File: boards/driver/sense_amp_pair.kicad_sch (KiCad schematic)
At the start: 18 parts, among them T15 1:1, T16 1:1, U9 SN7524

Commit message: Driver: Added a 5V->3.3V LDO to replace the reversed cmod header, added jumpers for the 200R parallel returns, and renamed subcircuit ports to avoid unexpected ground connections.
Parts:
- renumbered C32 to C41, C33 to C42, C34 to C43, C35 to C44, R59 to R241, R60 to R242, R61 to R243, R62 to R244, R63 to R245, R64 to R246, R65 to R247, R66 to R248, U9 to U8
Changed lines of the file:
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@@
   (symbol (lib_id "Device:R_US") (at 73.66 46.99 0)
     (in_bom yes) (on_board yes)
-    (property "Reference" "R59" (id 0) (at 75.3872 45.8216 0)
+    (property "Reference" "R241" (id 0) (at 75.3872 45.8216 0)
       (effects (font (size 1.27 1.27)) (justify left))
     )
@@
   (symbol (lib_id "Device:R_US") (at 73.66 57.15 0)
     (in_bom yes) (on_board yes)
-    (property "Reference" "R60" (id 0) (at 75.3872 55.9816 0)
+    (property "Reference" "R242" (id 0) (at 75.3872 55.9816 0)
       (effects (font (size 1.27 1.27)) (justify left))
     )
@@
   (symbol (lib_id "Device:R_US") (at 111.76 46.99 0) (mirror y)
     (in_bom yes) (on_board yes)
-    (property "Reference" "R63" (id 0) (at 106.68 45.72 0)
+    (property "Reference" "R245" (id 0) (at 106.68 45.72 0)
       (effects (font (size 1.27 1.27)) (justify right))
     )
@@
   (symbol (lib_id "Device:R_US") (at 111.76 57.15 0) (mirror y)
     (in_bom yes) (on_board yes)
-    (property "Reference" "R64" (id 0) (at 106.68 55.88 0)
+    (property "Reference" "R246" (id 0) (at 106.68 55.88 0)
       (effects (font (size 1.27 1.27)) (justify right))
     )
@@
   (symbol (lib_id "power:GND") (at 116.84 54.61 0)
     (in_bom yes) (on_board yes)
-    (property "Reference" "#PWR049" (id 0) (at 116.84 60.96 0)
+    (property "Reference" "#PWR0115" (id 0) (at 116.84 60.96 0)
       (effects (font (size 1.27 1.27)) hide)
     )
@@
   (symbol (lib_id "lachesis:SN7524") (at 142.24 52.07 0)
     (in_bom yes) (on_board yes)
-    (property "Reference" "U9" (id 0) (at 142.24 42.7482 0))
+    (property "Reference" "U8" (id 0) (at 142.24 42.7482 0))
     (property "Value" "SN7524" (id 1) (at 142.24 45.0596 0))
     (property "Footprint" "Package_DIP:DIP-16_W7.62mm_Socket" (id 2) (at 142.24 52.07 0)
@@
   (symbol (lib_id "Device:R_US") (at 73.66 72.39 0)
     (in_bom yes) (on_board yes)
-    (property "Reference" "R61" (id 0) (at 75.3872 71.2216 0)
+    (property "Reference" "R243" (id 0) (at 75.3872 71.2216 0)
       (effects (font (size 1.27 1.27)) (justify left))
     )
@@
   (symbol (lib_id "Device:R_US") (at 73.66 82.55 0)
     (in_bom yes) (on_board yes)
-    (property "Reference" "R62" (id 0) (at 75.3872 81.3816 0)
+    (property "Reference" "R244" (id 0) (at 75.3872 81.3816 0)
       (effects (font (size 1.27 1.27)) (justify left))
     )
@@
   (symbol (lib_id "Device:R_US") (at 111.76 72.39 0) (mirror y)
     (in_bom yes) (on_board yes)
-    (property "Reference" "R65" (id 0) (at 106.68 71.12 0)
+    (property "Reference" "R247" (id 0) (at 106.68 71.12 0)
       (effects (font (size 1.27 1.27)) (justify right))
     )
@@
   (symbol (lib_id "Device:R_US") (at 111.76 82.55 0) (mirror y)
     (in_bom yes) (on_board yes)
-    (property "Reference" "R66" (id 0) (at 106.68 81.28 0)
+    (property "Reference" "R248" (id 0) (at 106.68 81.28 0)
       (effects (font (size 1.27 1.27)) (justify right))
     )
@@
   (symbol (lib_id "power:GND") (at 116.84 80.01 0)
     (in_bom yes) (on_board yes)
-    (property "Reference" "#PWR050" (id 0) (at 116.84 86.36 0)
+    (property "Reference" "#PWR0116" (id 0) (at 116.84 86.36 0)
       (effects (font (size 1.27 1.27)) hide)
     )
@@
   (symbol (lib_id "lachesis:SN7524") (at 142.24 77.47 0)
     (in_bom yes) (on_board yes)
-    (property "Reference" "U9" (id 0) (at 142.24 68.1482 0))
+    (property "Reference" "U8" (id 0) (at 142.24 68.1482 0))
     (property "Value" "SN7524" (id 1) (at 142.24 70.4596 0))
     (property "Footprint" "Package_DIP:DIP-16_W7.62mm_Socket" (id 2) (at 142.24 77.47 0)
@@
       (effects (font (size 1.27 1.27)) hide)
     )
-    (pin "14")
-    (pin "15")
-    (pin "2")
-    (pin "3")
+    (pin "11")
+    (pin "12")
+    (pin "6")
+    (pin "7")
   )
   (symbol (lib_id "lachesis:Transformer_SP_SS") (at 92.71 77.47 0) (mirror x)
@@
   (symbol (lib_id "lachesis:SN7524") (at 205.74 85.09 0)
     (in_bom yes) (on_board yes)
-    (property "Reference" "U9" (id 0) (at 204.47 92.71 0)
+    (property "Reference" "U8" (id 0) (at 204.47 92.71 0)
       (effects (font (size 1.27 1.27)) (justify left))
     )
@@
       (effects (font (size 1.27 1.27)) hide)
     )
-    (pin "14")
-    (pin "15")
-    (pin "2")
-    (pin "3")
+    (pin "1")
+    (pin "10")
+    (pin "13")
+    (pin "16")
+    (pin "8")
+    (pin "9")
   )
   (symbol (lib_id "power:GND") (at 217.17 90.17 0)
     (in_bom yes) (on_board yes)
-    (property "Reference" "#PWR054" (id 0) (at 217.17 96.52 0)
+    (property "Reference" "#PWR0120" (id 0) (at 217.17 96.52 0)
       (effects (font (size 1.27 1.27)) hide)
     )
@@
   (symbol (lib_id "Device:C_Small") (at 217.17 85.09 180)
     (in_bom yes) (on_board yes)
-    (property "Reference" "C33" (id 0) (at 219.4814 83.9216 0)
+    (property "Reference" "C42" (id 0) (at 219.4814 83.9216 0)
       (effects (font (size 1.27 1.27)) (justify right))
     )
@@
   (symbol (lib_id "Device:C_Small") (at 226.06 81.28 0) (mirror y)
     (in_bom yes) (on_board yes)
-    (property "Reference" "C34" (id 0) (at 228.3968 82.4484 0)
+    (property "Reference" "C43" (id 0) (at 228.3968 82.4484 0)
       (effects (font (size 1.27 1.27)) (justify right))
     )
@@
   (symbol (lib_id "Device:C_Small") (at 226.06 93.98 0) (mirror y)
     (in_bom yes) (on_board yes)
-    (property "Reference" "C35" (id 0) (at 228.3968 95.1484 0)
+    (property "Reference" "C44" (id 0) (at 228.3968 95.1484 0)
       (effects (font (size 1.27 1.27)) (justify right))
     )
@@
   (symbol (lib_id "lachesis:SN7524") (at 140.97 113.03 0)
     (in_bom yes) (on_board yes)
-    (property "Reference" "U9" (id 0) (at 146.05 115.57 0))
+    (property "Reference" "U8" (id 0) (at 146.05 115.57 0))
     (property "Value" "SN7524" (id 1) (at 144.78 118.11 0))
     (property "Footprint" "Package_DIP:DIP-16_W7.62mm_Socket" (id 2) (at 140.97 113.03 0)
@@
       (effects (font (size 1.27 1.27)) hide)
     )
-    (pin "14")
-    (pin "15")
-    (pin "2")
-    (pin "3")
+    (pin "4")
+    (pin "5")
   )
   (symbol (lib_id "Device:C_Small") (at 129.54 113.03 0) (mirror x)
     (in_bom yes) (on_board yes)
-    (property "Reference" "C32" (id 0) (at 127.2286 111.8616 0)
+    (property "Reference" "C41" (id 0) (at 127.2286 111.8616 0)
       (effects (font (size 1.27 1.27)) (justify right))
     )
@@
   (symbol (lib_id "power:GND") (at 120.65 118.11 0)
     (in_bom yes) (on_board yes)
-    (property "Reference" "#PWR051" (id 0) (at 120.65 124.46 0)
+    (property "Reference" "#PWR0117" (id 0) (at 120.65 124.46 0)
       (effects (font (size 1.27 1.27)) hide)
     )
@@
   (symbol (lib_id "power:+5V") (at 203.2 72.39 0)
     (in_bom yes) (on_board yes)
-    (property "Reference" "#PWR052" (id 0) (at 203.2 76.2 0)
+    (property "Reference" "#PWR0118" (id 0) (at 203.2 76.2 0)
       (effects (font (size 1.27 1.27)) hide)
     )
@@
   (symbol (lib_id "power:-5V") (at 203.2 100.33 180)
     (in_bom yes) (on_board yes)
-    (property "Reference" "#PWR053" (id 0) (at 203.2 102.87 0)
-      (effects (font (size 1.27 1.27)) hide)
-    )
+    (property "Reference" "#PWR0119" (id 0) (at 203.2 102.87 0)
+      (effects (font (size 1.27 1.27)) hide)
+    )

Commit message: Driver: incorporated most changes from the test board, and began layout
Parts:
- C13: renamed from C41; value 10nF -> 0.01uF
- C15: renamed from C43; value 0.1uF -> 0.01uF
- C16: renamed from C44; value 0.1uF -> 0.01uF
- R189: renamed from R245; value 470 -> 100
- R190: renamed from R246; value 470 -> 100
- R191: renamed from R247; value 470 -> 100
- R192: renamed from R248; value 470 -> 100
- renumbered C42 to C14, R241 to R185, R242 to R186, R243 to R187, R244 to R188, T15 to T1, T16 to T2, U8 to U1
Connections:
- net +5V: now also U1.16 (VCC+)
- net -5V: now also U1.8 (VCC-)
- net GND: now also U1.13 (GND), U1.4 (-), U1.9 (GND); no longer U1.3
- net SAY: now also U1.12; no longer U1.14
- net SBF: now also U1.11; no longer U1.15
- net VREF: now also U1.5 (+); no longer U1.2
- net at R191.1, T2.4 (S2): now also U1.6; no longer U1.2
- net at R192.2, T2.6 (S1): now also U1.7; no longer U1.3
- net at C14.2: now also U1.1 (CEXT)

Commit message: Driver: laid out most of the subcircuits
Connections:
- net GARX: now also R187.1, T2.3 (P2); no longer R185.1, T1.3 (P2)
- net GARY: now also R185.1, T1.3 (P2); no longer R187.1, T2.3 (P2)
- net GBRX: now also R188.2, T2.1 (P1); no longer R186.2, T1.1 (P1)
- net GBRY: now also R186.2, T1.1 (P1); no longer R188.2, T2.1 (P1)
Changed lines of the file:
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@@
     (effects (font (size 1.27 1.27)) (justify right))
   )
-  (hierarchical_label "GARY" (shape input) (at 67.31 67.31 180)
+  (hierarchical_label "GARY" (shape input) (at 66.04 41.91 180)
     (effects (font (size 1.27 1.27)) (justify right))
   )
-  (hierarchical_label "GARX" (shape input) (at 66.04 41.91 180)
+  (hierarchical_label "GARX" (shape input) (at 67.31 67.31 180)
     (effects (font (size 1.27 1.27)) (justify right))
   )
-  (hierarchical_label "GBRX" (shape input) (at 67.31 62.23 180)
+  (hierarchical_label "GBRX" (shape input) (at 68.58 87.63 180)
     (effects (font (size 1.27 1.27)) (justify right))
   )
-  (hierarchical_label "GBRY" (shape input) (at 68.58 87.63 180)
+  (hierarchical_label "GBRY" (shape input) (at 67.31 62.23 180)
     (effects (font (size 1.27 1.27)) (justify right))
   )

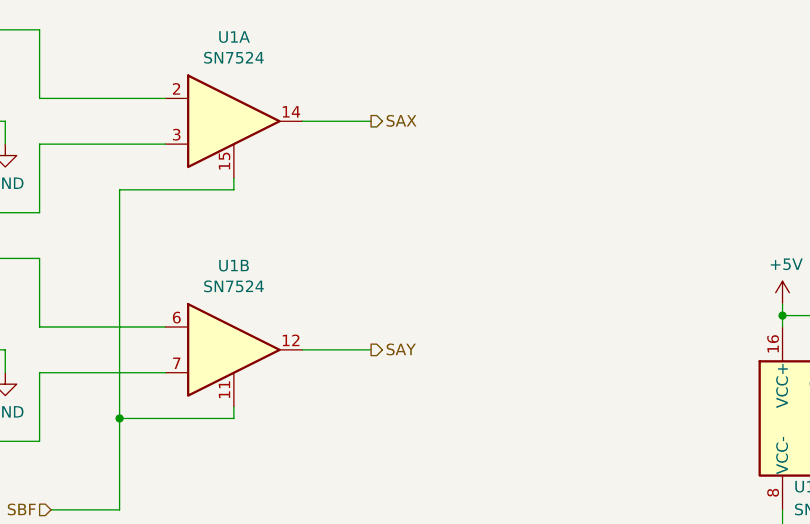
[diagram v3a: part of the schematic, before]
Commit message: Driver: almost totally rearranged 3.3V logic section. The ratsnest is now significantly detangled, and the FPGA routing is almost done. 89 nets left.
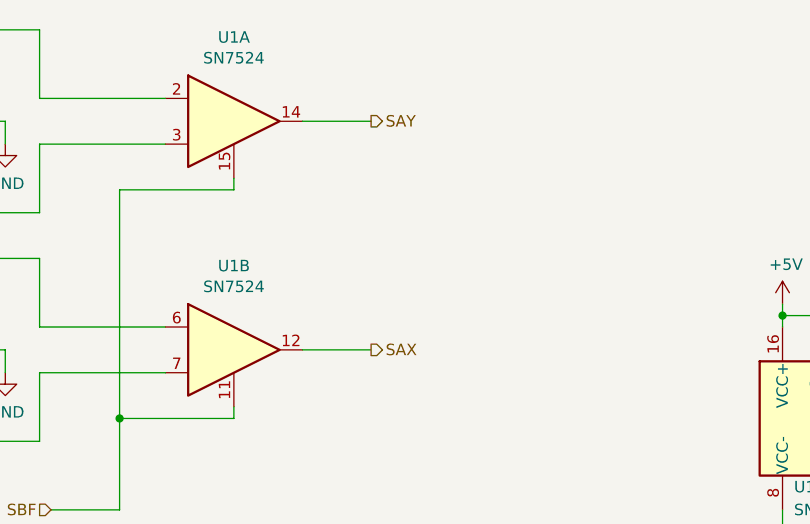
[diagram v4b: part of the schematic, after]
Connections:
- net SAX: now also U1.12; no longer U1.14
- net SAY: now also U1.14; no longer U1.12
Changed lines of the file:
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@@
     (effects (font (size 1.27 1.27)) (justify right))
   )
-  (hierarchical_label "SAY" (shape output) (at 157.48 77.47 0)
+  (hierarchical_label "SAY" (shape output) (at 157.48 52.07 0)
     (effects (font (size 1.27 1.27)) (justify left))
   )
-  (hierarchical_label "SAX" (shape output) (at 157.48 52.07 0)
+  (hierarchical_label "SAX" (shape output) (at 157.48 77.47 0)
     (effects (font (size 1.27 1.27)) (justify left))
   )

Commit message: Driver: minor schematic cleanup and populated all of the BOM except for resistors
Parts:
- C13: MPN (none) -> CL10B103KC8NNNC; Manufacturer (none) -> Samsung Electro-Mechanics; Package (none) -> 0603
- C14: MPN (none) -> CL10B101KB8NFNC; Manufacturer (none) -> Samsung Electro-Mechanics; Package (none) -> 0603
- C15, C16: MPN (none) -> CL10B103KC8NNNC; Manufacturer (none) -> Samsung Electro-Mechanics; Package (none) -> 0603; Rating (none) -> 100V; Tolerance (none) -> 10%
- T1, T2: MPN (none) -> 78615/1JC; Manufacturer (none) -> Murata Power Solutions, Inc; Package (none) -> 6 PIN SM
- U1: MPN (none) -> 110-93-316-41-001000; Manufacturer (none) -> Mill-Max Manufacturing Corp; Package (none) -> 16-DIP
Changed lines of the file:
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@@
+      (effects (font (size 1.27 1.27)) hide)
+    )
+    (property "MPN" "110-93-316-41-001000" (id 4) (at 142.24 52.07 0)
+      (effects (font (size 1.27 1.27)) hide)
+    )
+    (property "Description" "CONN IC DIP SOCKET 16POS GOLD" (id 5) (at 142.24 52.07 0)
+      (effects (font (size 1.27 1.27)) hide)
+    )
+    (property "Manufacturer" "Mill-Max Manufacturing Corp" (id 6) (at 142.24 52.07 0)
+      (effects (font (size 1.27 1.27)) hide)
+    )
+    (property "Package" "16-DIP" (id 7) (at 142.24 52.07 0)
       (effects (font (size 1.27 1.27)) hide)
     )
@@
       (effects (font (size 1.27 1.27)) hide)
     )
+    (property "MPN" "78615/1JC" (id 6) (at 92.71 52.07 0)
+      (effects (font (size 1.27 1.27)) hide)
+    )
+    (property "Manufacturer" "Murata Power Solutions, Inc" (id 7) (at 92.71 52.07 0)
+      (effects (font (size 1.27 1.27)) hide)
+    )
+    (property "Description" "PULSE XFMR 1CT:1CT 1.7MH" (id 8) (at 92.71 52.07 0)
+      (effects (font (size 1.27 1.27)) hide)
+    )
+    (property "Package" "6 PIN SM" (id 9) (at 92.71 52.07 0)
+      (effects (font (size 1.27 1.27)) hide)
+    )
     (pin "1")
     (pin "2")
@@
     )
     (property "Datasheet" "" (id 3) (at 142.24 77.47 0)
+      (effects (font (size 1.27 1.27)) hide)
+    )
+    (property "MPN" "110-93-316-41-001000" (id 4) (at 142.24 77.47 0)
+      (effects (font (size 1.27 1.27)) hide)
+    )
+    (property "Description" "CONN IC DIP SOCKET 16POS GOLD" (id 5) (at 142.24 77.47 0)
+      (effects (font (size 1.27 1.27)) hide)
+    )
+    (property "Manufacturer" "Mill-Max Manufacturing Corp" (id 6) (at 142.24 77.47 0)
+      (effects (font (size 1.27 1.27)) hide)
+    )
+    (property "Package" "16-DIP" (id 7) (at 142.24 77.47 0)
       (effects (font (size 1.27 1.27)) hide)
     )
@@
       (effects (font (size 1.27 1.27)) hide)
     )
+    (property "MPN" "78615/1JC" (id 6) (at 92.71 77.47 0)
+      (effects (font (size 1.27 1.27)) hide)
+    )
+    (property "Manufacturer" "Murata Power Solutions, Inc" (id 7) (at 92.71 77.47 0)
+      (effects (font (size 1.27 1.27)) hide)
+    )
+    (property "Description" "PULSE XFMR 1CT:1CT 1.7MH" (id 8) (at 92.71 77.47 0)
+      (effects (font (size 1.27 1.27)) hide)
+    )
+    (property "Package" "6 PIN SM" (id 9) (at 92.71 77.47 0)
+      (effects (font (size 1.27 1.27)) hide)
+    )
     (pin "1")
     (pin "2")
@@
     )
     (property "Datasheet" "" (id 3) (at 205.74 85.09 0)
+      (effects (font (size 1.27 1.27)) hide)
+    )
+    (property "MPN" "110-93-316-41-001000" (id 4) (at 205.74 85.09 0)
+      (effects (font (size 1.27 1.27)) hide)
+    )
+    (property "Description" "CONN IC DIP SOCKET 16POS GOLD" (id 5) (at 205.74 85.09 0)
+      (effects (font (size 1.27 1.27)) hide)
+    )
+    (property "Manufacturer" "Mill-Max Manufacturing Corp" (id 6) (at 205.74 85.09 0)
+      (effects (font (size 1.27 1.27)) hide)
+    )
+    (property "Package" "16-DIP" (id 7) (at 205.74 85.09 0)
       (effects (font (size 1.27 1.27)) hide)
     )
@@
       (effects (font (size 1.27 1.27)) hide)
     )
+    (property "Description" "CAP CER 100PF 50V X7R 0603" (id 8) (at 217.17 85.09 0)
+      (effects (font (size 1.27 1.27)) hide)
+    )
+    (property "MPN" "CL10B101KB8NFNC" (id 9) (at 217.17 85.09 0)
+      (effects (font (size 1.27 1.27)) hide)
+    )
+    (property "Manufacturer" "Samsung Electro-Mechanics" (id 10) (at 217.17 85.09 0)
+      (effects (font (size 1.27 1.27)) hide)
+    )
+    (property "Package" "0603" (id 11) (at 217.17 85.09 0)
+      (effects (font (size 1.27 1.27)) hide)
+    )
     (pin "1")
     (pin "2")
@@
       (effects (font (size 1.27 1.27)) hide)
     )
+    (property "Rating" "100V" (id 4) (at 226.06 81.28 0)
+      (effects (font (size 1.27 1.27)) hide)
+    )
+    (property "Tolerance" "10%" (id 5) (at 226.06 81.28 0)
+      (effects (font (size 1.27 1.27)) hide)
+    )
+    (property "Description" "CAP CER 10000PF 100V X7R 0603" (id 6) (at 226.06 81.28 0)
+      (effects (font (size 1.27 1.27)) hide)
+    )
+    (property "MPN" "CL10B103KC8NNNC" (id 7) (at 226.06 81.28 0)
+      (effects (font (size 1.27 1.27)) hide)
+    )
+    (property "Manufacturer" "Samsung Electro-Mechanics" (id 8) (at 226.06 81.28 0)
+      (effects (font (size 1.27 1.27)) hide)
+    )
+    (property "Package" "0603" (id 9) (at 226.06 81.28 0)
+      (effects (font (size 1.27 1.27)) hide)
+    )
     (pin "1")
     (pin "2")
@@
     )
     (property "Datasheet" "~" (id 3) (at 226.06 93.98 0)
+      (effects (font (size 1.27 1.27)) hide)
+    )
+    (property "Rating" "100V" (id 4) (at 226.06 93.98 0)
+      (effects (font (size 1.27 1.27)) hide)
+    )
+    (property "Tolerance" "10%" (id 5) (at 226.06 93.98 0)
+      (effects (font (size 1.27 1.27)) hide)
+    )
+    (property "Description" "CAP CER 10000PF 100V X7R 0603" (id 6) (at 226.06 93.98 0)
+      (effects (font (size 1.27 1.27)) hide)
+    )
+    (property "MPN" "CL10B103KC8NNNC" (id 7) (at 226.06 93.98 0)
+      (effects (font (size 1.27 1.27)) hide)
+    )
+    (property "Manufacturer" "Samsung Electro-Mechanics" (id 8) (at 226.06 93.98 0)
+      (effects (font (size 1.27 1.27)) hide)
+    )
+    (property "Package" "0603" (id 9) (at 226.06 93.98 0)
       (effects (font (size 1.27 1.27)) hide)
     )
@@
     )
     (property "Datasheet" "" (id 3) (at 140.97 113.03 0)
+      (effects (font (size 1.27 1.27)) hide)
+    )
+    (property "MPN" "110-93-316-41-001000" (id 4) (at 140.97 113.03 0)
+      (effects (font (size 1.27 1.27)) hide)
+    )
+    (property "Description" "CONN IC DIP SOCKET 16POS GOLD" (id 5) (at 140.97 113.03 0)
+      (effects (font (size 1.27 1.27)) hide)
+    )
+    (property "Manufacturer" "Mill-Max Manufacturing Corp" (id 6) (at 140.97 113.03 0)
+      (effects (font (size 1.27 1.27)) hide)
+    )
+    (property "Package" "16-DIP" (id 7) (at 140.97 113.03 0)
       (effects (font (size 1.27 1.27)) hide)
     )
@@
       (effects (font (size 1.27 1.27)) hide)
     )
+    (property "Description" "CAP CER 10000PF 100V X7R 0603" (id 8) (at 129.54 113.03 0)
+      (effects (font (size 1.27 1.27)) hide)
+    )
+    (property "MPN" "CL10B103KC8NNNC" (id 9) (at 129.54 113.03 0)
+      (effects (font (size 1.27 1.27)) hide)
+    )
+    (property "Manufacturer" "Samsung Electro-Mechanics" (id 10) (at 129.54 113.03 0)
+      (effects (font (size 1.27 1.27)) hide)
+    )
+    (property "Package" "0603" (id 11) (at 129.54 113.03 0)
+      (effects (font (size 1.27 1.27)) hide)
+    )
